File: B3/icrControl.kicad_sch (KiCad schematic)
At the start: 11 parts, among them U329 74HC00, U330 74HC74, U331 74HC74, U332 74HC74, U333 74HC74, U334 74HC74, U335 74HC04, U336 74HC244, U337 74HC08, U338 74HC32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

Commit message: .
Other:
- company: (none) -> Daniel Molina
- title: (none) -> 74HCT6526 Board 3
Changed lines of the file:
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@@
 (kicad_sch (version 20211123) (generator eeschema)
   (paper "A4")
+  (title_block
+    (title "74HCT6526 Board 3")
+    (date "2022-10-08")
+    (rev "0.1.2")
+    (company "Daniel Molina")
+    (comment 1 "https://github.com/dmolinagarcia/74HCT6526")
+  )
   (junction (at 33.02 21.59) (diameter 0) (color 0 0 0 0)
   )

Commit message: .
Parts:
- removed unit 3 of U335
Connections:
- net ~{SDRIRQ}: now reaches U331.10 (~{S})
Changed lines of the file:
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@@
     (stroke (width 0) (type default) (color 0 0 0 0))
   )
-  (wire (pts (xy 105.41 109.22) (xy 110.49 109.22))
+  (wire (pts (xy 105.41 109.22) (xy 125.73 109.22))
     (stroke (width 0) (type default) (color 0 0 0 0))
   )
@@
     (effects (font (size 1.27 1.27)) (justify right))
   )
-  (hierarchical_label "SDRIRQ" (shape input) (at 105.41 109.22 180)
+  (hierarchical_label "~{SDRIRQ}" (shape input) (at 105.41 109.22 180)
     (effects (font (size 1.27 1.27)) (justify right))
   )
@@
     (pin "11")
     (pin "12")
-    (pin "13")
-    (pin "14")
-    (pin "7")
-  )
-  (symbol (lib_id "74xx:74HC04") (at 118.11 109.22 0) (unit 3)
-    (in_bom yes) (on_board yes)
-    (property "Reference" "U335" (id 0) (at 121.92 104.14 0))
-    (property "Value" "74HC04" (id 1) (at 121.92 106.68 0))
-    (property "Footprint" "Package_SO:SO-14_3.9x8.65mm_P1.27mm" (id 2) (at 118.11 109.22 0)
-      (effects (font (size 1.27 1.27)) hide)
-    )
-    (property "Datasheet" "https://assets.nexperia.com/documents/data-sheet/74HC_HCT04.pdf" (id 3) (at 118.11 109.22 0)
-      (effects (font (size 1.27 1.27)) hide)
-    )
-    (pin "1")
-    (pin "2")
-    (pin "3")
-    (pin "4")
-    (pin "5")
-    (pin "6")
-    (pin "8")
-    (pin "9")
-    (pin "10")
-    (pin "11")
-    (pin "12")

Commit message: B0 ready for v0.2.0 release.
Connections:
- net at U333.10 (~{S}), U333.6 (~{Q}): no longer U333.1 (~{R})
- net at U333.8 (~{Q}): now also U333.1 (~{R})
- no-connect marks 9 -> 8
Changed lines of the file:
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@@
   (title_block
     (title "74HCT6526 Board 3")
-    (date "2022-10-08")
-    (rev "0.1.2")
+    (date "2023-01-22")
+    (rev "0.2.0")
     (company "Daniel Molina")
     (comment 1 "https://github.com/dmolinagarcia/74HCT6526")
@@
   )
   (junction (at 88.9 73.66) (diameter 0) (color 0 0 0 0)
-  )
-  (junction (at 137.16 142.24) (diameter 0) (color 0 0 0 0)
   )
   (junction (at 118.11 114.3) (diameter 0) (color 0 0 0 0)
@@
   (no_connect (at 76.2 68.58))
   (no_connect (at 133.35 137.16))
-  (no_connect (at 157.48 142.24))
   (no_connect (at 133.35 96.52))
   (bus_entry (at 229.87 52.07) (size 2.54 -2.54)
@@
     (stroke (width 0) (type default) (color 0 0 0 0))
   )
+  (wire (pts (xy 160.02 142.24) (xy 157.48 142.24))
+    (stroke (width 0) (type default) (color 0 0 0 0))
+  )
   (bus (pts (xy 232.41 49.53) (xy 232.41 52.07))
     (stroke (width 0) (type default) (color 0 0 0 0))
@@
     (stroke (width 0) (type default) (color 0 0 0 0))
   )
-  (wire (pts (xy 125.73 147.32) (xy 137.16 147.32))
-    (stroke (width 0) (type default) (color 0 0 0 0))
-  )
   (wire (pts (xy 33.02 34.29) (xy 33.02 31.75))
     (stroke (width 0) (type default) (color 0 0 0 0))
@@
     (stroke (width 0) (type default) (color 0 0 0 0))
   )
+  (wire (pts (xy 125.73 148.59) (xy 160.02 148.59))
+    (stroke (width 0) (type default) (color 0 0 0 0))
+  )
   (bus (pts (xy 157.48 95.25) (xy 157.48 109.22))
     (stroke (width 0) (type default) (color 0 0 0 0))
@@
     (stroke (width 0) (type default) (color 0 0 0 0))
   )
-  (wire (pts (xy 137.16 147.32) (xy 137.16 142.24))
-    (stroke (width 0) (type default) (color 0 0 0 0))
-  )
   (bus (pts (xy 173.99 134.62) (xy 173.99 137.16))
     (stroke (width 0) (type default) (color 0 0 0 0))
@@
     (stroke (width 0) (type default) (color 0 0 0 0))
   )
+  (wire (pts (xy 125.73 147.32) (xy 125.73 148.59))
+    (stroke (width 0) (type default) (color 0 0 0 0))
+  )
   (wire (pts (xy 160.02 39.37) (xy 200.66 39.37))
     (stroke (width 0) (type default) (color 0 0 0 0))
@@
     (stroke (width 0) (type default) (color 0 0 0 0))
   )
+  (wire (pts (xy 160.02 148.59) (xy 160.02 142.24))
+    (stroke (width 0) (type default) (color 0 0 0 0))
+  )
   (wire (pts (xy 160.02 92.71) (xy 187.96 92.71))
     (stroke (width 0) (type default) (color 0 0 0 0))
@@
     (effects (font (size 1.27 1.27)) (justify left bottom))
   )
+  (label "~{ICRCLR}" (at 104.14 149.86 0)
+    (effects (font (size 1.27 1.27)) (justify left bottom))
+  )

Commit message: Ready for v0.2.1
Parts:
- added SW301: SW_SPDT, Button_Switch_SMD:SW_SPDT_PCM12, symbol Switch:SW_SPDT
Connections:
- net ~{IRQ}: now also SW301.2 (B); no longer U334.8 (~{Q})
- net at U334.6 (~{Q}): now also SW301.1 (A)
- new net: SW301.3 (C), U334.8 (~{Q})
- no-connect marks 8 -> 7
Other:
- moved on the sheet: U334A, U334B, U335D

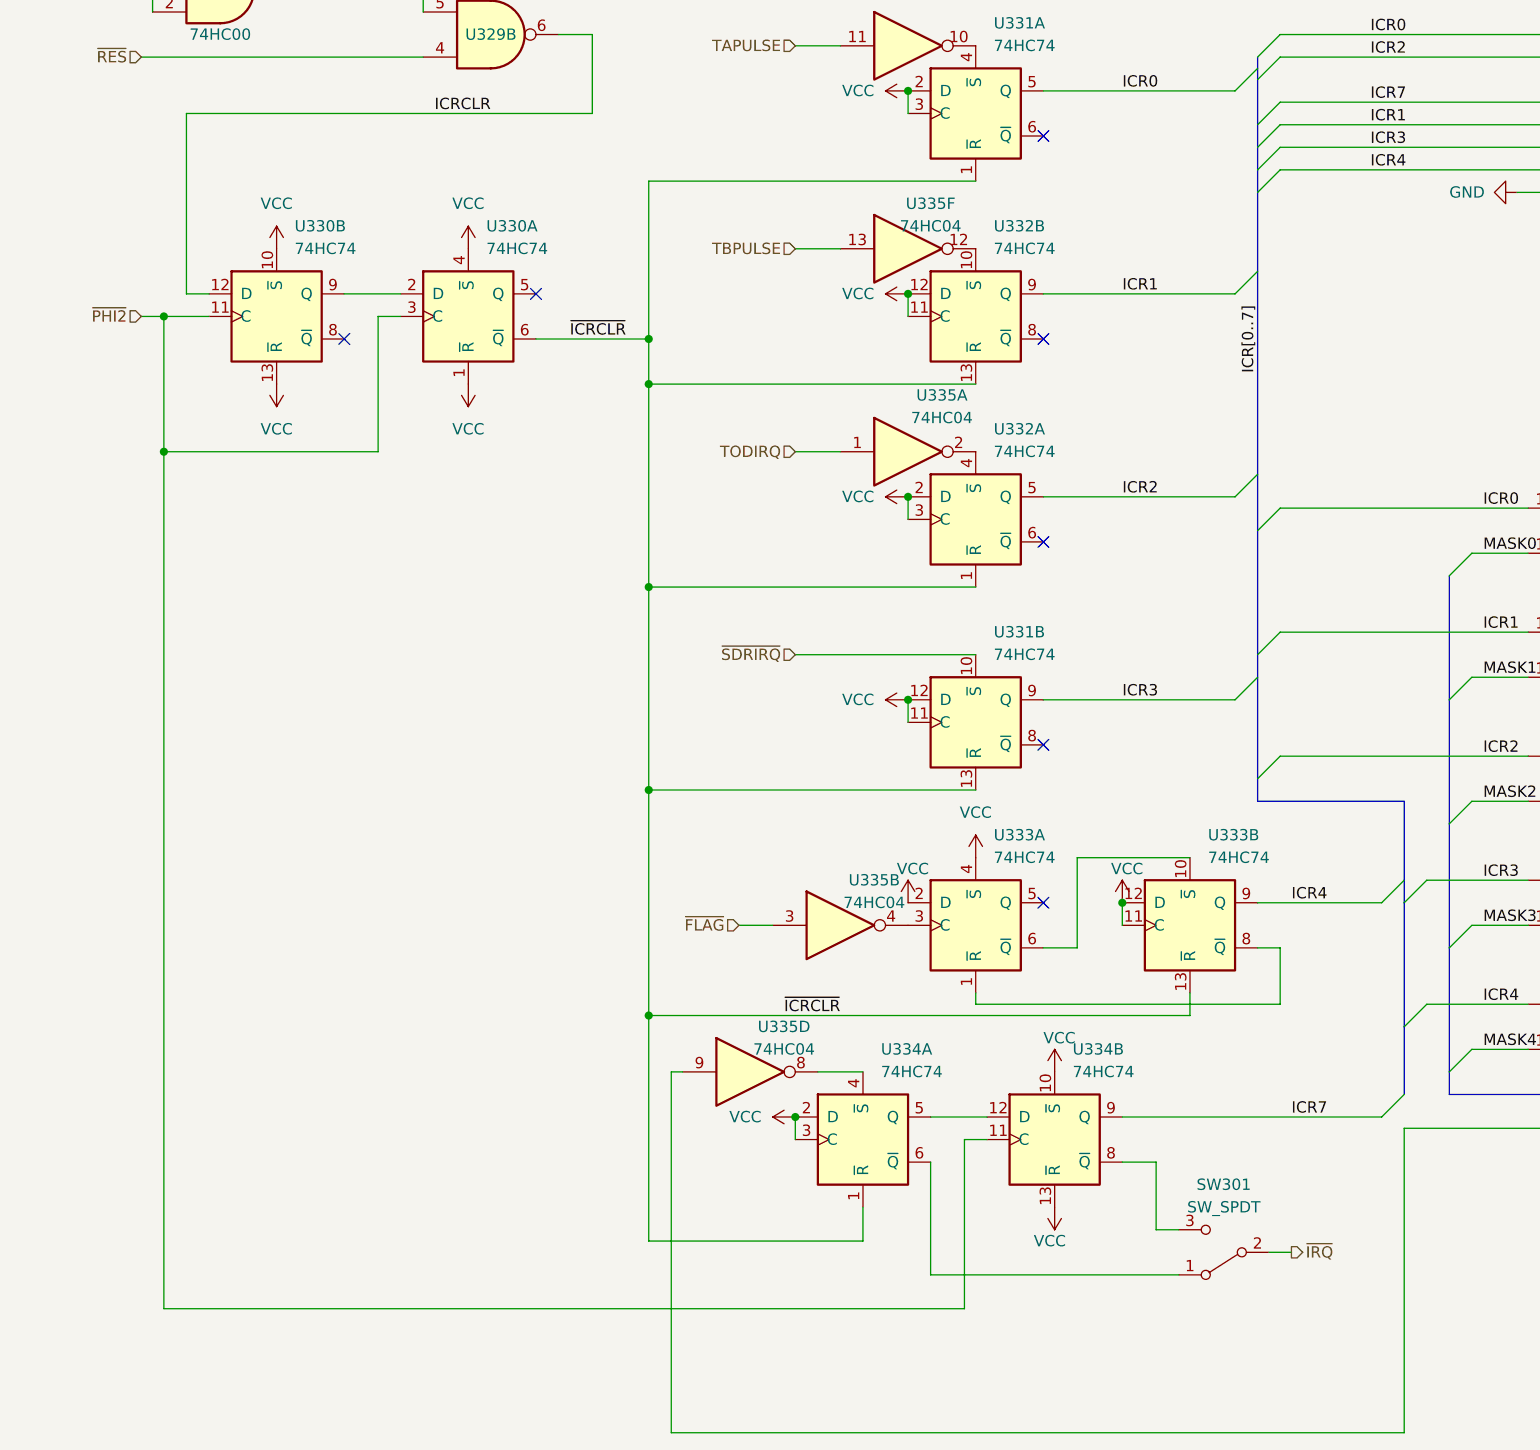
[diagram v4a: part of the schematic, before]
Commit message: Issue #12 diagnosis
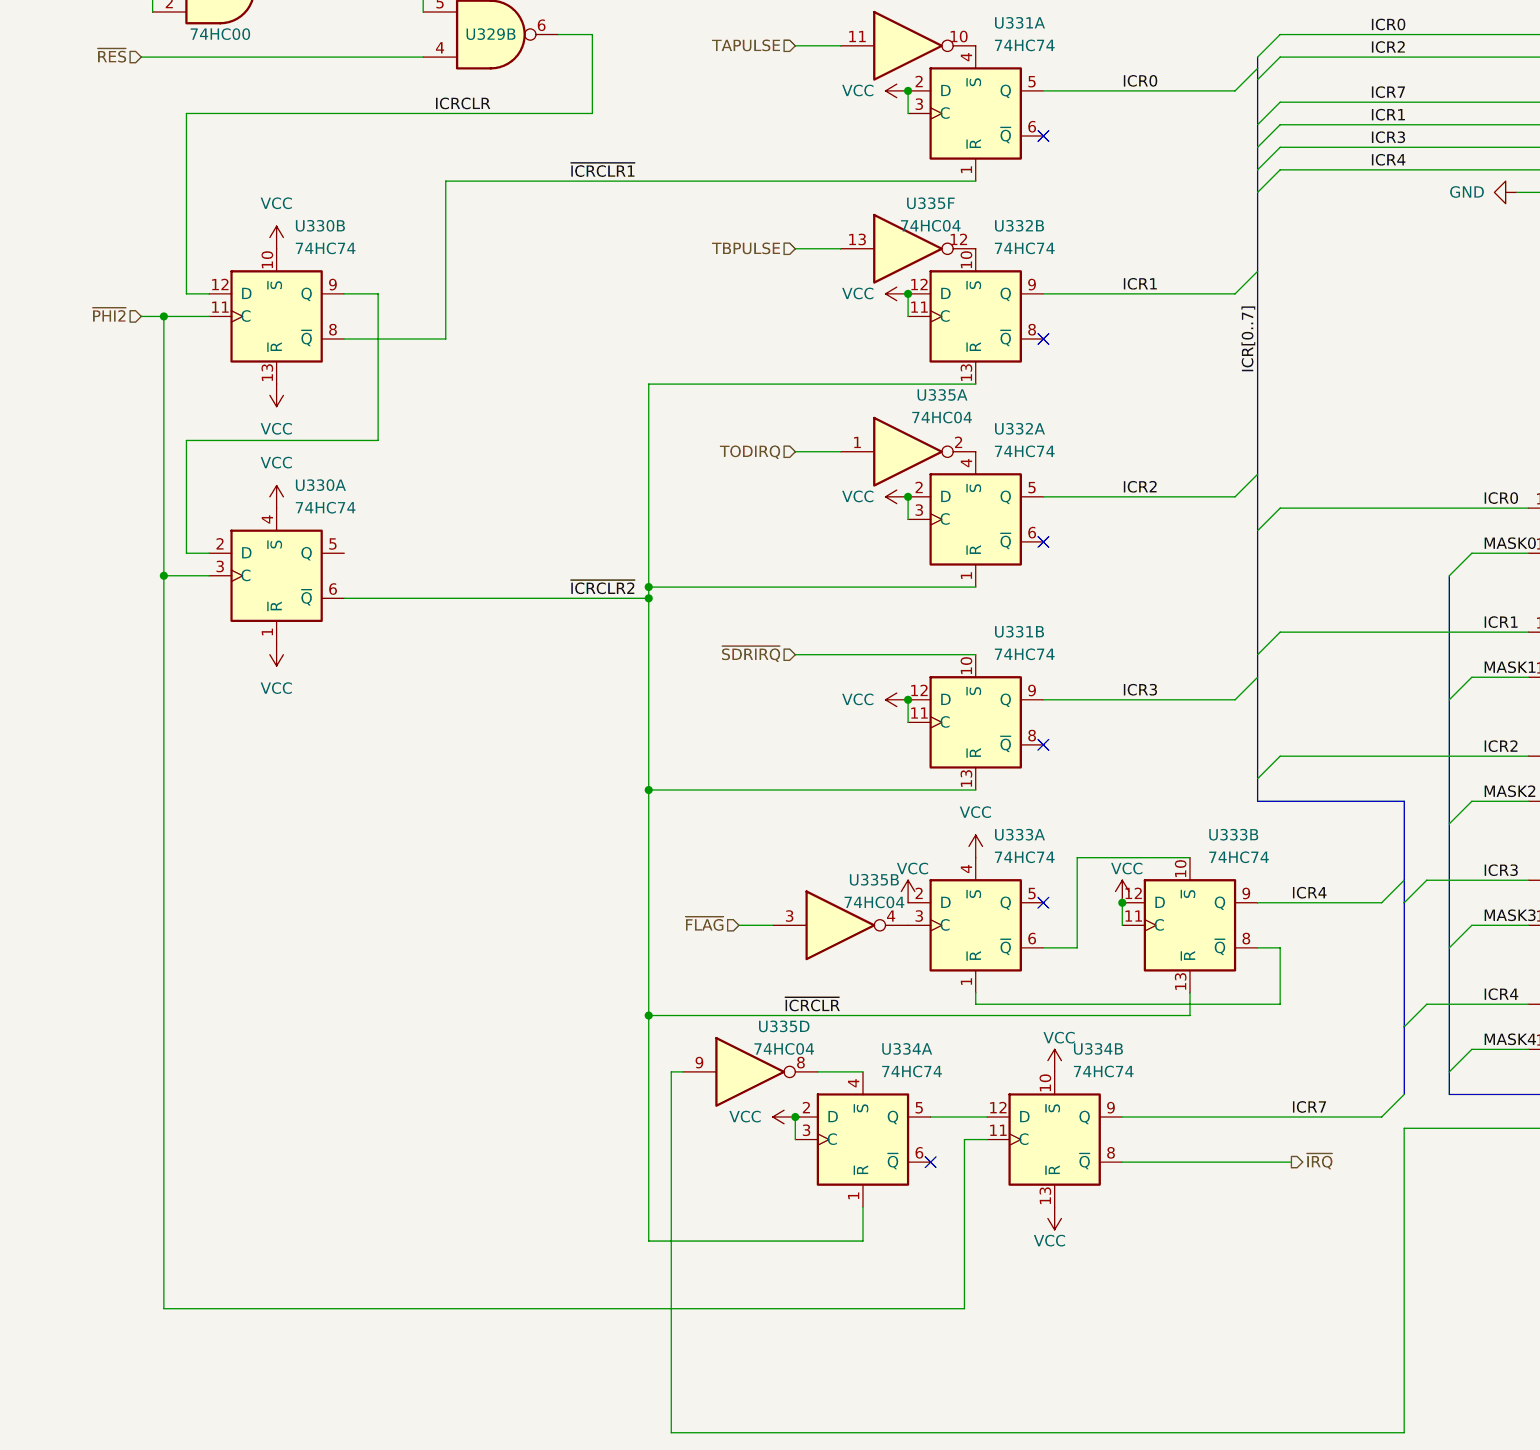
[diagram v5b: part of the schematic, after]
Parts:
- removed SW301: SW_SPDT, Button_Switch_SMD:SW_SPDT_PCM12, symbol Switch:SW_SPDT
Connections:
- net ~{IRQ}: now also U334.8 (~{Q})
- net ~{ICRCLR1}: now reaches U330.8 (~{Q})
- net ~{ICRCLR1}: now also U331.1 (~{R})
- net ~{ICRCLR} renamed ~{ICRCLR2}
- net ~{ICRCLR2}: no longer U331.1 (~{R})
- no-connect marks 7 -> 6
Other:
- moved on the sheet: U330A
